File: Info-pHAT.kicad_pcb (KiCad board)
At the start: 2 copper layers, 65 x 30 mm, 22 parts, among them U1 CAT24C32WI-GT3

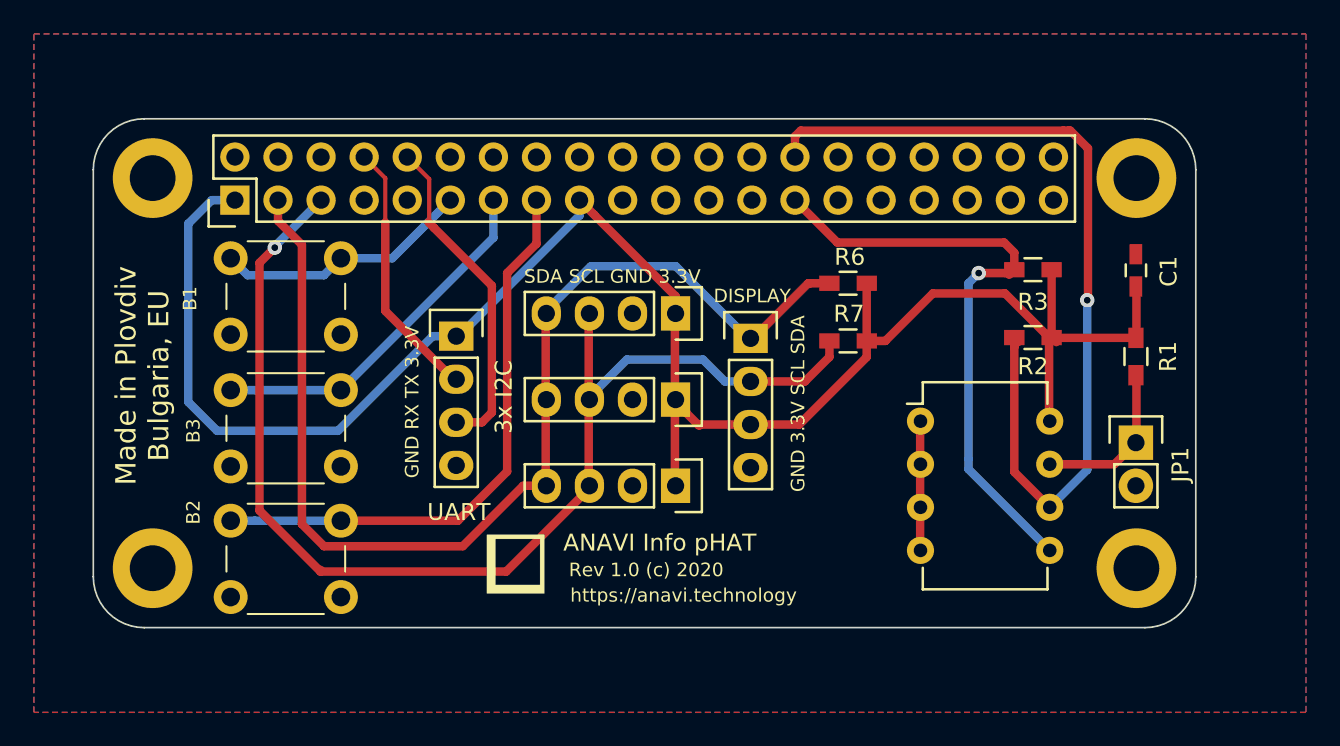
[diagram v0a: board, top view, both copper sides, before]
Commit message: Info-pHAT.pro: Add LED D1 and D2
Add indication LEDs D1 and D2.

Signed-off-by: Leon Anavi <leon@anavi.org>
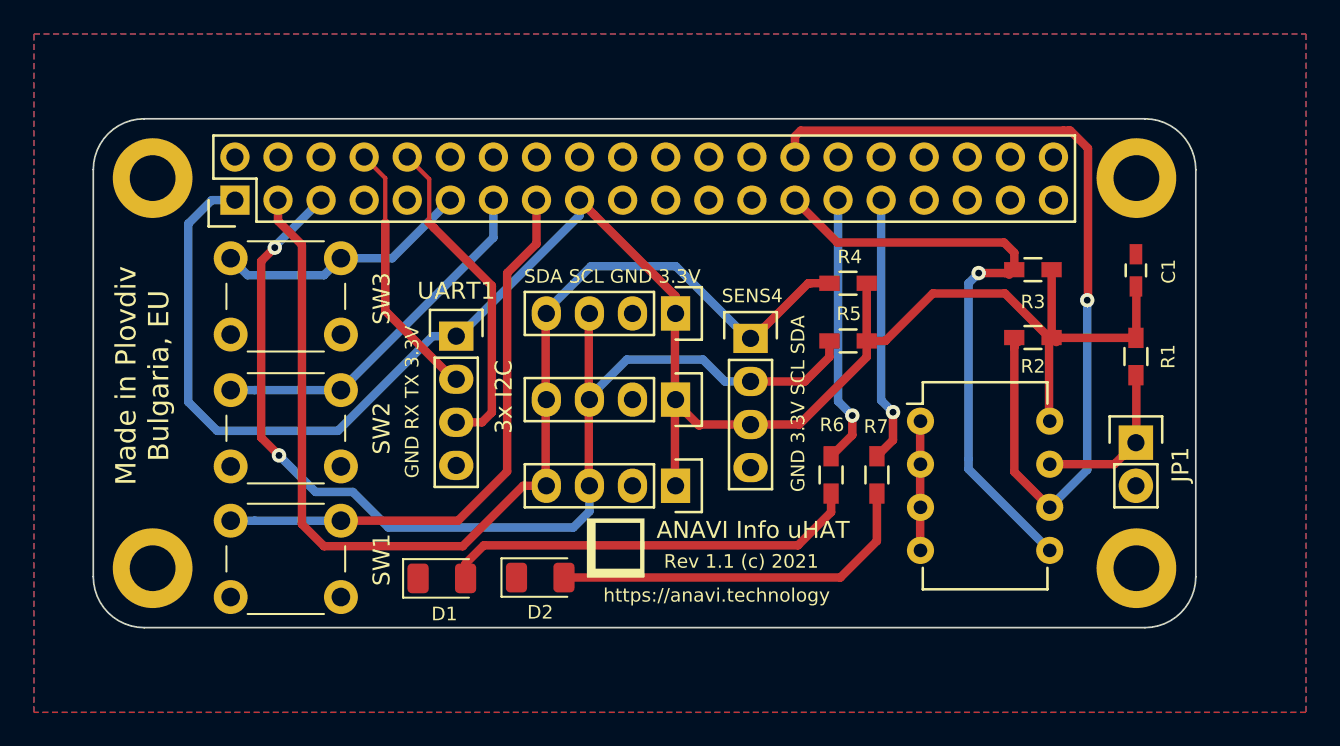
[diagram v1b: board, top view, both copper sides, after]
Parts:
- removed B2: SW_DIP_x01, Buttons_Switches_ThroughHole:SW_PUSH_6mm_h4.3mm
- added D1: LED, LED_SMD:LED_1206_3216Metric, F.Cu at (169.1, 102.1)
- added D2: LED, LED_SMD:LED_1206_3216Metric, F.Cu at (174.8, 102.0)
- added R6: 270R, Resistors_SMD:R_0603_HandSoldering, F.Cu at (192.0, 96.0)
- added R7: 270R, Resistors_SMD:R_0603_HandSoldering, F.Cu at (194.7, 96.0)
- added SW1: SW_DIP_x01, Buttons_Switches_ThroughHole:SW_PUSH_6mm_h4.3mm, F.Cu at (156.6, 98.7)
- moved ? 5.98 mm to (179.3, 100.3)
- renumbered R6 to R4, R7 to R5, DISPLAY to SENS4, B3 to SW2, B1 to SW3, UART to UART1
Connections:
- RASP_CONN1 pad 29: (no net) -> Net-(R6-Pad2)
- RASP_CONN1 pad 31: (no net) -> Net-(R7-Pad2)
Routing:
- net Net-(D1-Pad2): track 0.00 -> 24.8 mm
- net Net-(D2-Pad2): track 0.00 -> 22.1 mm
- net Net-(R6-Pad2): track 0.00 -> 16.0 mm, vias 0 -> 1
- net Net-(R7-Pad2): track 0.00 -> 15.8 mm, vias 0 -> 1
- net Net-(R5-Pad2): track 70.8 -> 66.8 mm, vias 1 -> 2
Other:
- board text added: "ANAVI Info uHAT"
- board text added: "Rev 1.1 (c) 2021"
- board text removed: "ANAVI Info pHAT"
- board text removed: "Rev 1.0 (c) 2020"

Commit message: Info-pHAT.kicad_pcb: Update labels
Update labels and adjust positions.

Signed-off-by: Leon Anavi <leon@anavi.org>
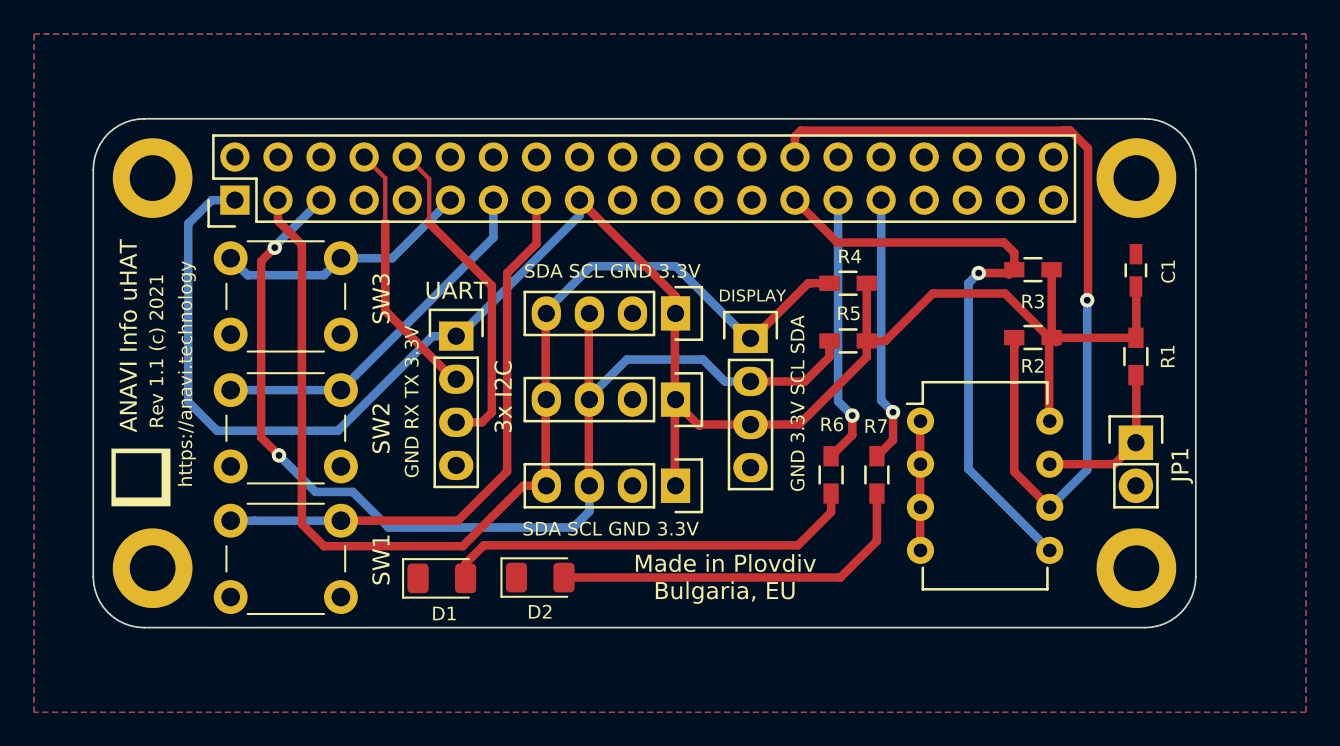
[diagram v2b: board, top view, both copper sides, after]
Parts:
- moved ? 28.3 mm to (151.3, 96.2), turned to 90 degrees
- renumbered SENS4 to DISPLAY, UART1 to UART

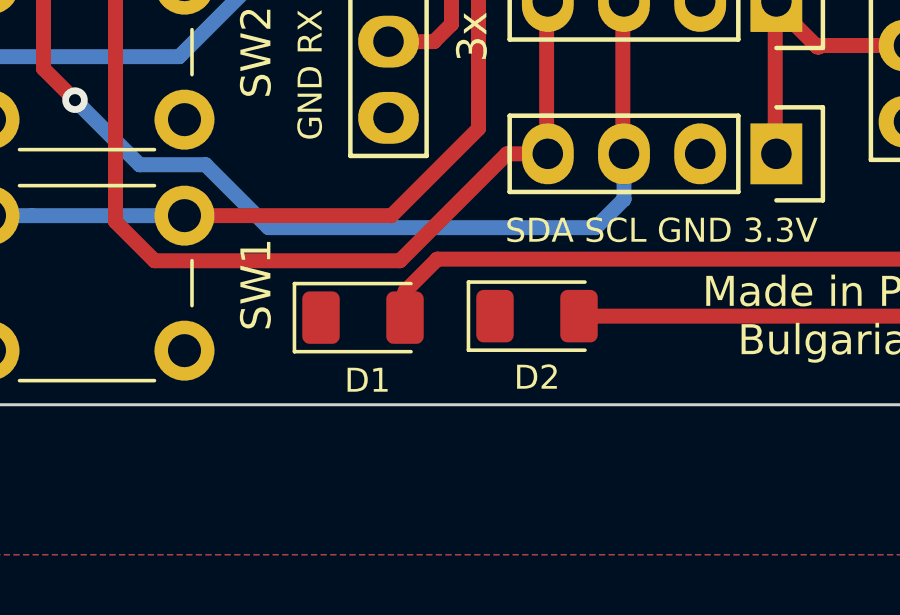
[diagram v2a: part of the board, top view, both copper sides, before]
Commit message: Info-pHAT.kicad_pcb: Add a label
Add a label for the direction of the LEDs.

Signed-off-by: Leon Anavi <leon@anavi.org>
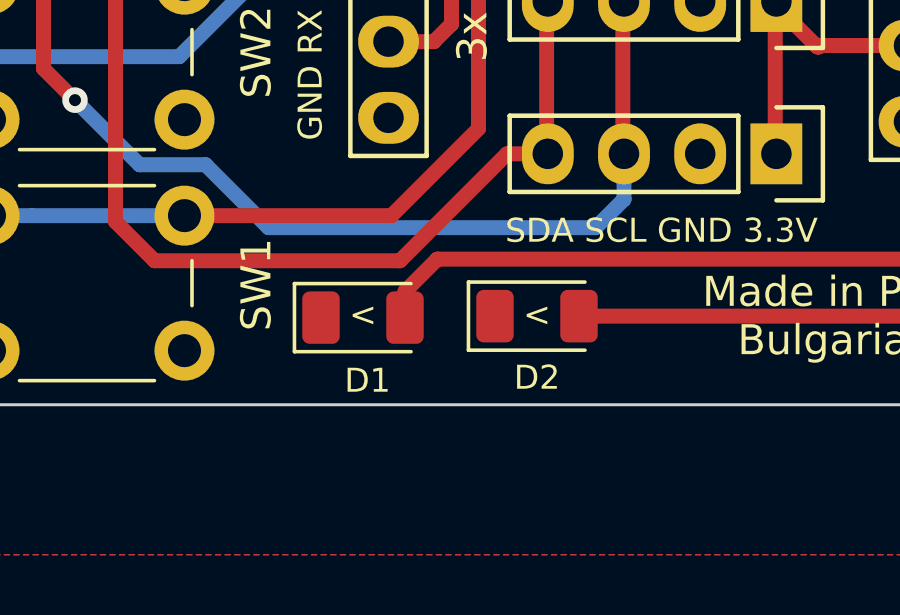
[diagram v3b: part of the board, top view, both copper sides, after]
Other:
- board text added: "<"
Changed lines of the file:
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@@
   (general
     (thickness 1.6)
-    (drawings 27)
+    (drawings 29)
     (tracks 220)
     (zones 0)
@@
       (drillshape 0)
       (scaleselection 1)
-      (outputdirectory "plots/rev11/"))
+      (outputdirectory "plots/rev11a/"))
   )
   (net 0 "")
@@
     )
   )
+  (gr_text < (at 174.85 102) (layer F.SilkS)
+    (effects (font (size 0.8 0.8) (thickness 0.1)))
+  )
+  (gr_text < (at 169.05 102) (layer F.SilkS)
+    (effects (font (size 0.8 0.8) (thickness 0.1)))
+  )
   (gr_text "SDA SCL GND 3.3V" (at 179 99.2) (layer F.SilkS)

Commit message: Info-pHAT.kicad_pcb: Add assembly details
Add details for the assembly to the fabrication layer.

Signed-off-by: Leon Anavi <leon@anavi.org>
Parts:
- D1: value LED -> KP-3216EC
- D2: value LED -> KP-3216SGC
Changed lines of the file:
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@@
       (effects (font (size 0.8 0.8) (thickness 0.15)))
     )
-    (fp_text value LED (at -0.05 -2) (layer F.Fab)
-      (effects (font (size 1 1) (thickness 0.15)))
+    (fp_text value KP-3216EC (at -0.05 -2) (layer F.Fab)
+      (effects (font (size 0.6 0.6) (thickness 0.15)))
     )
     (fp_line (start 1.6 -0.8) (end -1.2 -0.8) (layer F.Fab) (width 0.1))
@@
       (effects (font (size 0.8 0.8) (thickness 0.15)))
     )
-    (fp_text value LED (at -0.1 -1.95) (layer F.Fab)
-      (effects (font (size 1 1) (thickness 0.15)))
+    (fp_text value KP-3216SGC (at -0.1 -1.95) (layer F.Fab)
+      (effects (font (size 0.6 0.6) (thickness 0.15)))
     )
     (fp_text user %R (at 0 0) (layer F.Fab)
@@
       (effects (font (size 0.8 0.8) (thickness 0.1)))
     )
-    (fp_text value 270R (at 0.1 0.05 90) (layer F.Fab)
-      (effects (font (size 1 1) (thickness 0.15)))
+    (fp_text value 270R (at -3.05 -0.9 180) (layer F.Fab)
+      (effects (font (size 0.8 0.8) (thickness 0.1)))
     )
     (fp_line (start -2 -0.8) (end 2 -0.8) (layer F.CrtYd) (width 0.05))
@@
       (effects (font (size 0.8 0.8) (thickness 0.1)))
     )
-    (fp_text value 270R (at 0.05 0.05 90) (layer F.Fab)
-      (effects (font (size 1 1) (thickness 0.15)))
+    (fp_text value 270R (at -3 0.15 180) (layer F.Fab)
+      (effects (font (size 0.8 0.8) (thickness 0.1)))
     )
     (fp_line (start -0.5 -0.675) (end 0.5 -0.675) (layer F.SilkS) (width 0.15))
